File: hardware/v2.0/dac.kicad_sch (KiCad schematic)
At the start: 1 part, among them IC3 LTC2630ISC6-LZ12#TRMPBF

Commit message: DAC Vout
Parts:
- added C82: 100n, Capacitor_SMD:C_0402_1005Metric, symbol Device:C
- added J8: 530480210, 530480210:MOLEX_530480210, symbol 530480210:530480210
- added U1: ECP5U-25F-CABGA256, Package_BGA:BGA-256_14.0x14.0mm_Layout16x16_P0.8mm_Ball0.45mm_Pad0.32mm_NSMD, symbol icepi-lib:LFE5U-25F-6BG256x
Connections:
- net ~{CS}(DAC): now reaches IC3.1 (~{CS}/LD)
- net ~{CS}(DAC): now also U1.C12 (PT56B/-)
- net SCK: now reaches IC3.2 (SCK)
- net SCK: now also U1.D13 (PT62A/+)
- net SDI: now reaches IC3.3 (SDI)
- net SDI: now also U1.E12 (PT58B/-)
- net +3V3: now reaches IC3.4 (VCC)
- net +3V3: now also C82.1
- net GND: now reaches IC3.5 (GND)
- net GND: now also C82.2, J8.2
- net VOUT(DAC): now reaches IC3.6 (VOUT)
- net VOUT(DAC): now also J8.1
- no-connect marks 0 -> 1
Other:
- moved on the sheet: IC3

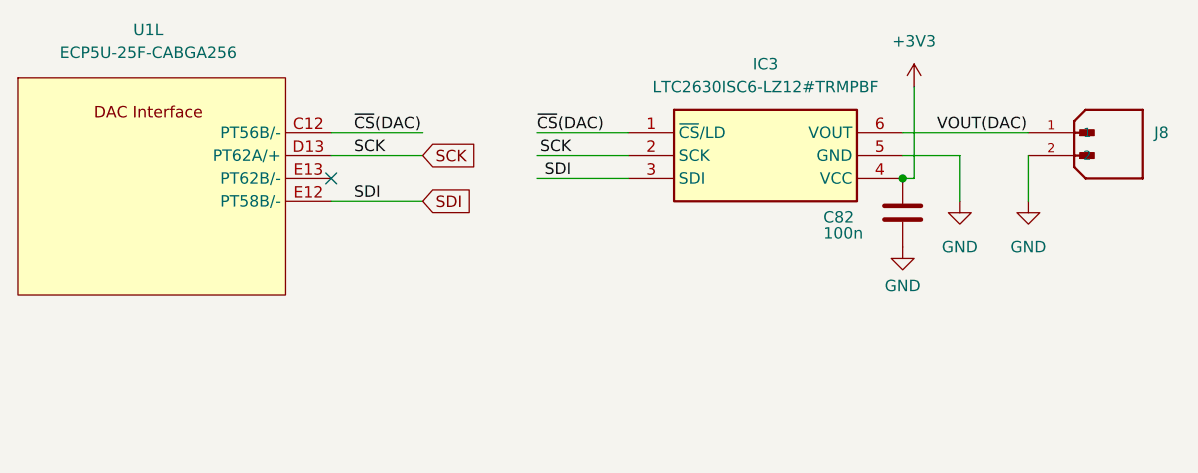
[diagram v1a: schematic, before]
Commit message: Logo fix
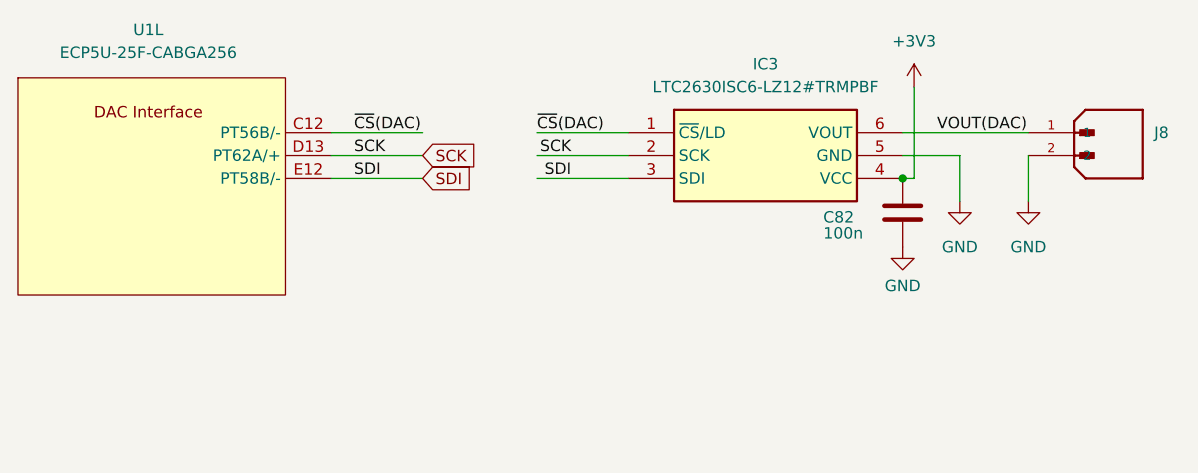
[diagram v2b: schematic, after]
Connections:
- no-connect marks 1 -> 0
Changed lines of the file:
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@@
 		(color 0 0 0 0)
-	)
-	(no_connect
-		(at 125.73 97.79)
 	)
 	(wire
@@
 	(wire
 		(pts
-			(xy 125.73 100.33) (xy 135.89 100.33)
+			(xy 125.73 97.79) (xy 135.89 97.79)
 		)
 		(stroke
@@
 	)
 	(label "SDI"
-		(at 128.27 100.33 0)
+		(at 128.27 97.79 0)
 		(effects
 			(font
@@
 	(global_label "SDI"
 		(shape input)
-		(at 135.89 100.33 0)
+		(at 135.89 97.79 0)
 		(fields_autoplaced yes)
 		(effects
@@
 		)
 		(property "Intersheetrefs" "${INTERSHEET_REFS}"
-			(at 141.9595 100.33 0)
+			(at 141.9595 97.79 0)
 			(effects
 				(font
@@
 		(pin "C12"
 		)
-		(pin "E13"
-		)
 		(pin "D12"

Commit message: ERC pass
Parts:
- IC3: MANUFACTURER (none) -> ADI; MANUFACTURER_PART_NUMBER (none) -> LTC2630ISC6-LZ12#TRMPBF
- J8: MANUFACTURER_PART_NUMBER (none) -> 0530480210
- U1: MANUFACTURER (none) -> Lattice; MANUFACTURER_PART_NUMBER (none) -> LFE5U-25F-6BG256C
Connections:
- net SCK: no longer U1.D13 (PT62A/+)
- net SDI: no longer U1.E12 (PT58B/-)
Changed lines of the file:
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@@
+	(wire
+		(pts
+			(xy 148.59 95.25) (xy 158.75 95.25)
+		)
+		(stroke
+			(width 0)
+			(type default)
+		)
+	)
+	(wire
+		(pts
+			(xy 148.59 97.79) (xy 158.75 97.79)
+		)
+		(stroke
+			(width 0)
+			(type default)
+		)
+	)
+	(wire
+		(pts
+			(xy 189.23 97.79) (xy 190.5 97.79)
+		)
+		(stroke
+			(width 0)
+			(type default)
+		)
+	)
+	(wire
+		(pts
+			(xy 189.23 92.71) (xy 203.2 92.71)
+		)
+		(stroke
+			(width 0)
+			(type default)
+		)
+	)
+	(wire
+		(pts
+			(xy 203.2 100.33) (xy 203.2 95.25)
+		)
+		(stroke
+			(width 0)
+			(type default)
+		)
+	)
+	(wire
+		(pts
+			(xy 148.59 92.71) (xy 158.75 92.71)
+		)
+		(stroke
+			(width 0)
+			(type default)
+		)
+	)
 	(wire
 		(pts
@@
 	(wire
 		(pts
-			(xy 125.73 95.25) (xy 135.89 95.25)
+			(xy 195.58 95.25) (xy 195.58 100.33)
 		)
 		(stroke
@@
 	(wire
 		(pts
-			(xy 148.59 95.25) (xy 158.75 95.25)
+			(xy 189.23 95.25) (xy 195.58 95.25)
 		)
 		(stroke
 			(width 0)
 			(type default)
-		)
-	)
-	(wire
-		(pts
-			(xy 148.59 97.79) (xy 158.75 97.79)
-		)
-		(stroke
-			(width 0)
-			(type default)
-		)
-	)
-	(wire
-		(pts
-			(xy 189.23 97.79) (xy 190.5 97.79)
-		)
-		(stroke
-			(width 0)
-			(type default)
-		)
-	)
-	(wire
-		(pts
-			(xy 189.23 92.71) (xy 203.2 92.71)
-		)
-		(stroke
-			(width 0)
-			(type default)
-		)
-	)
-	(wire
-		(pts
-			(xy 203.2 100.33) (xy 203.2 95.25)
-		)
-		(stroke
-			(width 0)
-			(type default)
-		)
-	)
-	(wire
-		(pts
-			(xy 148.59 92.71) (xy 158.75 92.71)
-		)
-		(stroke
-			(width 0)
-			(type default)
-		)
-	)
-	(wire
-		(pts
-			(xy 125.73 92.71) (xy 135.89 92.71)
-		)
-		(stroke
-			(width 0)
-			(type default)
-		)
-	)
-	(wire
-		(pts
-			(xy 195.58 95.25) (xy 195.58 100.33)
-		)
-		(stroke
-			(width 0)
-			(type default)
-		)
-	)
-	(wire
-		(pts
-			(xy 189.23 95.25) (xy 195.58 95.25)
-		)
-		(stroke
-			(width 0)
-			(type default)
-		)
-	)
-	(label "SDI"
-		(at 128.27 97.79 0)
-		(effects
-			(font
-				(size 1.27 1.27)
-			)
-			(justify left bottom)
 		)
 	)
@@
 	)
 	(label "~{CS}(DAC)"
-		(at 128.27 92.71 0)
+		(at 128.27 97.79 0)
 		(effects
 			(font
@@
 		)
 	)
-	(label "SCK"
-		(at 128.27 95.25 0)
-		(effects
-			(font
-				(size 1.27 1.27)
-			)
-			(justify left bottom)
-		)
-	)
 	(label "SDI"
 		(at 152.4 97.79 180)
@@
 	(global_label "SCK"
 		(shape input)
-		(at 135.89 95.25 0)
+		(at 148.59 95.25 180)
 		(fields_autoplaced yes)
 		(effects
@@
 				(size 1.27 1.27)
 			)
-			(justify left)
+			(justify right)
 		)
 		(property "Intersheetrefs" "${INTERSHEET_REFS}"
-			(at 142.6247 95.25 0)
-			(effects
-				(font
-					(size 1.27 1.27)
-				)
-				(justify left)
+			(at 141.8553 95.25 0)
+			(effects
+				(font
+					(size 1.27 1.27)
+				)
+				(justify right)
 				(hide yes)
 			)
@@
 	(global_label "SDI"
 		(shape input)
-		(at 135.89 97.79 0)
+		(at 148.59 97.79 180)
 		(fields_autoplaced yes)
 		(effects
@@
 				(size 1.27 1.27)
 			)
-			(justify left)
+			(justify right)
 		)
 		(property "Intersheetrefs" "${INTERSHEET_REFS}"
-			(at 141.9595 97.79 0)
-			(effects
-				(font
-					(size 1.27 1.27)
-				)
-				(justify left)
+			(at 142.5205 97.79 0)
+			(effects
+				(font
+					(size 1.27 1.27)
+				)
+				(justify right)
 				(hide yes)
 			)
@@
 			)
 		)
+		(property "MANUFACTURER" "ADI"
+			(at 158.75 92.71 0)
+			(effects
+				(font
+					(size 1.27 1.27)
+				)
+				(hide yes)
+			)
+		)
+		(property "MANUFACTURER_PART_NUMBER" "LTC2630ISC6-LZ12#TRMPBF"
+			(at 158.75 92.71 0)
+			(effects
+				(font
+					(size 1.27 1.27)
+				)
+				(hide yes)
+			)
+		)
 		(pin "6"
 		)
@@
 			)
 		)
-		(property "Description" ""
+		(property "Description" "Connector Header Through Hole, Right Angle 2 position 0.049\" (1.25mm)"
 			(at 208.28 92.71 0)
 			(effects
@@
 				)
 				(justify bottom)
+				(hide yes)
+			)
+		)
+		(property "MANUFACTURER_PART_NUMBER" "0530480210"
+			(at 208.28 92.71 0)
+			(effects
+				(font
+					(size 1.27 1.27)
+				)
 				(hide yes)
 			)
@@
 			)
 		)
+		(property "MANUFACTURER" "Lattice"
+			(at 105.41 110.49 0)
+			(effects
+				(font
+					(size 1.27 1.27)
+				)
+				(hide yes)
+			)
+		)
+		(property "MANUFACTURER_PART_NUMBER" "LFE5U-25F-6BG256C"
+			(at 105.41 110.49 0)
+			(effects
+				(font
+					(size 1.27 1.27)
+				)
+				(hide yes)
+			)
+		)
 		(pin "M5"
 		)
@@
 		(pin "D13"
 		)
+		(pin "P2"
+		)
+		(pin "P1"
+		)
+		(pin "G13"
+		)
+		(pin "E15"
+		)
+		(pin "N1"
+		)
 		(pin "E12"
 		)
-		(pin "D13"
-		)
-		(pin "P2"
-		)
-		(pin "P1"
-		)
-		(pin "G13"
-		)
-		(pin "E15"
-		)
-		(pin "N1"
-		)
-		(pin "E12"
-		)
 		(pin "G12"
 		)
@@
 		(pin "P4"
 		)
-		(pin "N6"
-		)
 		(pin "K5"
